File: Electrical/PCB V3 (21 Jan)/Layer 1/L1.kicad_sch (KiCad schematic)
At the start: 198 parts, among them J1 Conn_01x02, J3 Conn_01x02, SW1 SW_SPDT, U2 CD74HC4067SM, U3 CD74HC4067SM, U4 XT30UPB-M, U5 113991054

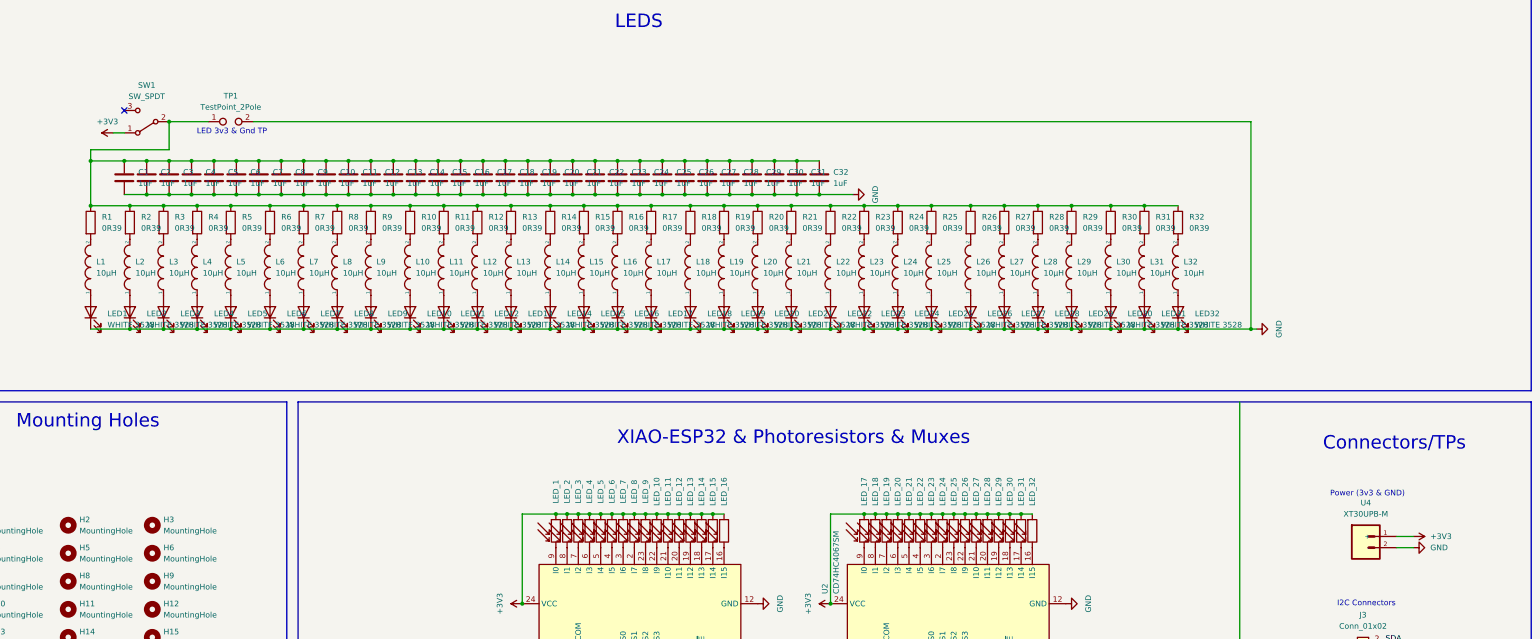
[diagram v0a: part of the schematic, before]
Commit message: added l2 dxf v4, started on l1 again
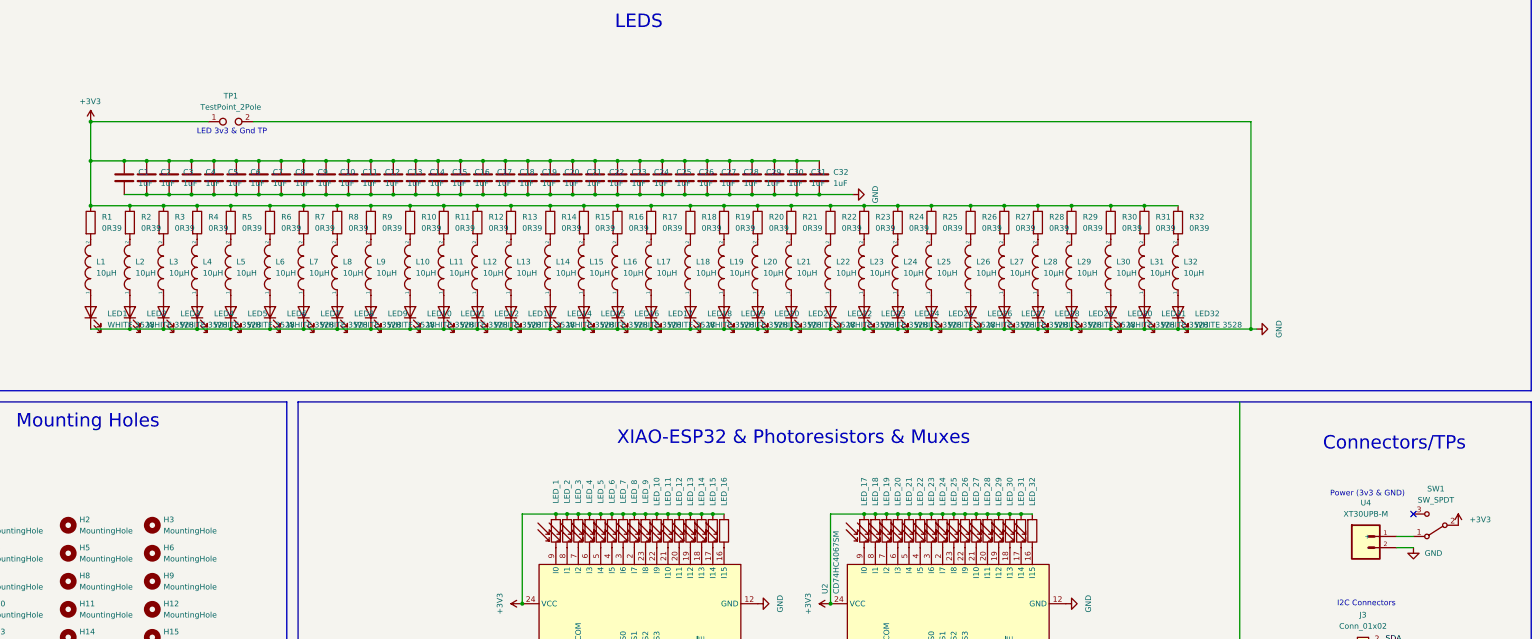
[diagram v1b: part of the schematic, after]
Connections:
- net +3V3: now also C1.1, C10.1, C11.1, C12.1, C13.1, C14.1, C15.1, C16.1, C17.1, C18.1, C19.1, C2.1, C20.1, C21.1, C22.1, C23.1, C24.1, C25.1, C26.1, C27.1, C28.1, C29.1, C3.1, C30.1, C31.1, C32.1, C4.1, C5.1, C6.1, C7.1, C8.1, C9.1, R1.1, R10.1, R11.1, R12.1, R13.1, R14.1, R15.1, R16.1, R17.1, R18.1, R19.1, R2.1, R20.1, R21.1, R22.1, R23.1, R24.1, R25.1, R26.1, R27.1, R28.1, R29.1, R3.1, R30.1, R31.1, R32.1, R4.1, R5.1, R6.1, R7.1, R8.1, R9.1, SW1.2 (B), TP1.1; no longer SW1.1 (A), U4.1 (+)
- new net: SW1.1 (A), U4.1 (+)
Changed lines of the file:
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@@
 	)
 	(junction
-		(at 90.17 53.34)
-		(diameter 0)
-		(color 0 0 0 0)
-	)
-	(junction
 		(at 191.77 62.23)
 		(diameter 0)
@@
 	)
 	(junction
+		(at 72.39 53.34)
+		(diameter 0)
+		(color 0 0 0 0)
+	)
+	(junction
 		(at 283.21 142.24)
 		(diameter 0)
@@
 	)
 	(no_connect
-		(at 80.01 50.8)
-	)
-	(no_connect
 		(at 210.82 175.26)
 	)
@@
 		(at 245.11 218.44)
 	)
+	(no_connect
+		(at 372.11 142.24)
+	)
 	(wire
 		(pts
@@
 	(wire
 		(pts
-			(xy 72.39 59.69) (xy 90.17 59.69)
-		)
-		(stroke
-			(width 0)
-			(type default)
-		)
-	)
-	(wire
-		(pts
-			(xy 99.06 53.34) (xy 90.17 53.34)
-		)
-		(stroke
-			(width 0)
-			(type default)
-		)
-	)
-	(wire
-		(pts
 			(xy 120.65 69.85) (xy 125.73 69.85)
 		)
@@
 	(wire
 		(pts
-			(xy 90.17 53.34) (xy 90.17 59.69)
-		)
-		(stroke
-			(width 0)
-			(type default)
-		)
-	)
-	(wire
-		(pts
 			(xy 88.9 100.33) (xy 96.52 100.33)
 		)
@@
 	(wire
 		(pts
-			(xy 72.39 59.69) (xy 72.39 62.23)
+			(xy 72.39 53.34) (xy 72.39 62.23)
 		)
 		(stroke
@@
 	(wire
 		(pts
+			(xy 72.39 53.34) (xy 99.06 53.34)
+		)
+		(stroke
+			(width 0)
+			(type default)
+		)
+	)
+	(wire
+		(pts
 			(xy 335.28 100.33) (xy 336.55 100.33)
 		)
@@
 	(wire
 		(pts
-			(xy 77.47 55.88) (xy 80.01 55.88)
-		)
-		(stroke
-			(width 0)
-			(type default)
-		)
-	)
-	(wire
-		(pts
 			(xy 191.77 72.39) (xy 199.39 72.39)
 		)
@@
 	)
 	(symbol
+		(lib_id "Switch:SW_SPDT")
+		(at 377.19 144.78 180)
+		(unit 1)
+		(exclude_from_sim no)
+		(in_bom yes)
+		(on_board yes)
+		(dnp no)
+		(fields_autoplaced yes)
+		(property "Reference" "SW1"
+			(at 377.19 136.525 0)
+			(effects
+				(font
+					(size 1.27 1.27)
+				)
+			)
+		)
+		(property "Value" "SW_SPDT"
+			(at 377.19 139.065 0)
+			(effects
+				(font
+					(size 1.27 1.27)
+				)
+			)
+		)
+		(property "Footprint" "Button_Switch_SMD:Nidec_Copal_CAS-120A"
+			(at 377.19 144.78 0)
+			(effects
+				(font
+					(size 1.27 1.27)
+				)
+				(hide yes)
+			)
+		)
+		(property "Datasheet" "~"
+			(at 377.19 144.78 0)
+			(effects
+				(font
+					(size 1.27 1.27)
+				)
+				(hide yes)
+			)
+		)
+		(property "Description" ""
+			(at 377.19 144.78 0)
+			(effects
+				(font
+					(size 1.27 1.27)
+				)
+				(hide yes)
+			)
+		)
+		(pin "2"
+		)
+		(pin "1"
+		)
+		(pin "3"
+		)
+		(instances
+			(project "L1"
+				(path "/9e8a7821-ee65-4356-a785-1f444d794ef4"
+					(reference "SW1")
+					(unit 1)
+				)
+			)
+		)
+	)
+	(symbol
 		(lib_id "Device:R_Photo")
 		(at 180.34 146.05 0)
@@
 	(symbol
 		(lib_id "power:+3V3")
-		(at 372.11 147.32 270)
+		(at 382.27 144.78 0)
 		(unit 1)
 		(exclude_from_sim no)
@@
 		(fields_autoplaced yes)
 		(property "Reference" "#PWR03"
-			(at 368.3 147.32 0)
+			(at 382.27 148.59 0)
 			(effects
 				(font
@@
 		)
 		(property "Value" "+3V3"
-			(at 375.92 147.3199 90)
+			(at 384.81 143.5099 0)
 			(effects
 				(font
@@
 		)
 		(property "Footprint" ""
-			(at 372.11 147.32 0)
+			(at 382.27 144.78 0)
 			(effects
 				(font
@@
 		)
 		(property "Datasheet" ""
-			(at 372.11 147.32 0)
+			(at 382.27 144.78 0)
 			(effects
 				(font
@@
 		)
 		(property "Description" "Power symbol creates a global label with name \"+3V3\""
-			(at 372.11 147.32 0)
+			(at 382.27 144.78 0)
 			(effects
 				(font
@@
 	(symbol
 		(lib_id "Library:GND")
-		(at 372.11 149.86 90)
+		(at 372.11 149.86 0)
 		(unit 1)
 		(exclude_from_sim no)
@@
 		(fields_autoplaced yes)
 		(property "Reference" "#PWR04"
-			(at 378.46 149.86 0)
+			(at 372.11 156.21 0)
 			(effects
 				(font
@@
 		)
 		(property "Value" "GND"
-			(at 375.92 149.8599 90)
+			(at 374.65 151.1299 0)
 			(effects
 				(font
 					(size 1.27 1.27)
 				)
-				(justify right)
+				(justify left)
 			)
 		)
@@
 	)
 	(symbol
-		(lib_id "Switch:SW_SPDT")
-		(at 85.09 53.34 180)
-		(unit 1)
-		(exclude_from_sim no)
-		(in_bom yes)
-		(on_board yes)
-		(dnp no)
-		(fields_autoplaced yes)
-		(property "Reference" "SW1"
-			(at 85.09 45.085 0)
-			(effects
-				(font
-					(size 1.27 1.27)
-				)
-			)
-		)
-		(property "Value" "SW_SPDT"
-			(at 85.09 47.625 0)
-			(effects
-				(font
-					(size 1.27 1.27)
-				)
-			)
-		)
-		(property "Footprint" "Button_Switch_SMD:Nidec_Copal_CAS-120A"
-			(at 85.09 53.34 0)
-			(effects
-				(font
-					(size 1.27 1.27)
-				)
-				(hide yes)
-			)
-		)
-		(property "Datasheet" "~"
-			(at 85.09 53.34 0)
-			(effects
-				(font
-					(size 1.27 1.27)
-				)
-				(hide yes)
-			)
-		)
-		(property "Description" ""
-			(at 85.09 53.34 0)
-			(effects
-				(font
-					(size 1.27 1.27)
-				)
-				(hide yes)
-			)
-		)
-		(pin "2"
-		)
-		(pin "1"
-		)
-		(pin "3"
-		)
-		(instances
-			(project "l1 v1"
-				(path "/9e8a7821-ee65-4356-a785-1f444d794ef4"
-					(reference "SW1")
-					(unit 1)
-				)
-			)
-		)
-	)
-	(symbol
 		(lib_id "Device:C")
 		(at 135.89 66.04 0)
@@
 	(symbol
 		(lib_id "power:+3V3")
-		(at 77.47 55.88 90)
+		(at 72.39 53.34 0)
 		(unit 1)
 		(exclude_from_sim no)
@@
 		(on_board yes)
 		(dnp no)
-		(fields_autoplaced yes)
 		(property "Reference" "#PWR09"
-			(at 81.28 55.88 0)
+			(at 72.39 57.15 0)
 			(effects
 				(font
@@
 		)
 		(property "Value" "+3V3"
-			(at 76.2 53.34 90)
+			(at 69.85 48.768 0)
 			(effects
 				(font
 					(size 1.27 1.27)
 				)
+				(justify left)
 			)
 		)
 		(property "Footprint" ""
-			(at 77.47 55.88 0)
+			(at 72.39 53.34 0)
 			(effects
 				(font
@@
 		)
 		(property "Datasheet" ""
-			(at 77.47 55.88 0)
+			(at 72.39 53.34 0)
 			(effects
 				(font
@@
 		)
 		(property "Description" "Power symbol creates a global label with name \"+3V3\""
-			(at 77.47 55.88 0)
+			(at 72.39 53.34 0)
 			(effects
 				(font

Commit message: finished l1?
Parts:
- J1, J3, TP1: footprint Connector_PinHeader_1.00mm:PinHeader_1x02_P1.00mm_Vertical -> Connector_PinHeader_2.54mm:PinHeader_1x02_P2.54mm_Vertical
- R33, R34: footprint Resistor_SMD:R_0201_0603Metric -> Resistor_SMD:R_0603_1608Metric
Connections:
- net Mux Com (1-16): now also R34.2, U3.1 (COM), U5.2 (D1); no longer R33.2, U2.1 (COM), U5.1 (D0)
- net Mux Com (17-32): now also R33.2, U2.1 (COM), U5.1 (D0); no longer R34.2, U3.1 (COM), U5.2 (D1)
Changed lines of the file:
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@@
 	)
 	(label "Mux Com (17-32)"
-		(at 175.26 175.26 270)
+		(at 245.11 176.53 270)
 		(effects
 			(font
@@
 	)
 	(label "Mux Com (17-32)"
-		(at 209.55 215.9 180)
+		(at 209.55 213.36 180)
 		(effects
 			(font
@@
 	)
 	(label "Mux Com (1-16)"
-		(at 209.55 213.36 180)
+		(at 209.55 215.9 180)
 		(effects
 			(font
@@
 	)
 	(label "Mux Com (1-16)"
-		(at 245.11 176.53 270)
+		(at 175.26 175.26 270)
 		(effects
 			(font
@@
 			)
 		)
-		(property "Footprint" "Resistor_SMD:R_0201_0603Metric"
+		(property "Footprint" "Resistor_SMD:R_0603_1608Metric"
 			(at 184.658 179.07 90)
 			(effects
@@
 			)
 		)
-		(property "Footprint" "Connector_PinHeader_1.00mm:PinHeader_1x02_P1.00mm_Vertical"
+		(property "Footprint" "Connector_PinHeader_2.54mm:PinHeader_1x02_P2.54mm_Vertical"
 			(at 104.14 53.34 0)
 			(effects
@@
 			)
 		)
-		(property "Footprint" "Resistor_SMD:R_0201_0603Metric"
+		(property "Footprint" "Resistor_SMD:R_0603_1608Metric"
 			(at 254.508 180.34 90)
 			(effects
@@
 			)
 		)
-		(property "Footprint" "Connector_PinHeader_1.00mm:PinHeader_1x02_P1.00mm_Vertical"
+		(property "Footprint" "Connector_PinHeader_2.54mm:PinHeader_1x02_P2.54mm_Vertical"
 			(at 360.68 196.85 0)
 			(effects
@@
 			)
 		)
-		(property "Footprint" "Connector_PinHeader_1.00mm:PinHeader_1x02_P1.00mm_Vertical"
+		(property "Footprint" "Connector_PinHeader_2.54mm:PinHeader_1x02_P2.54mm_Vertical"
 			(at 360.68 173.99 0)
 			(effects

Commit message: finished layer1?
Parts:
- added C33, C34: C, Capacitor_SMD:C_0603_1608Metric, symbol Device:C
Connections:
- net +3V3: now also C33.1, C34.1; no longer U2.24 (VCC), U3.24 (VCC)
- new net: C33.2, U3.24 (VCC)
- new net: C34.2, U2.24 (VCC)
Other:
- moved on the sheet: LED_1, LED_10, LED_11, LED_12, LED_13, LED_14, LED_15, LED_16, LED_17, LED_18, LED_19, LED_2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

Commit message: added l3 v3 dxf, did somemore l1
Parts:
- removed J1, J3: Conn_01x02, Connector_PinHeader_2.54mm:PinHeader_1x02_P2.54mm_Vertical, symbol Connector_Generic:Conn_01x02
- removed SW1: SW_SPDT, Button_Switch_SMD:Nidec_Copal_CAS-120A, symbol Switch:SW_SPDT
- removed U4: XT30UPB-M, Connector_AMASS:AMASS_XT30U-M_1x02_P5.0mm_Vertical, symbol XT30UPB-M:XT30UPB-M
- added J1: Conn_01x04, Connector_JST:JST_EH_B4B-EH-A_1x04_P2.50mm_Vertical, symbol Connector_Generic:Conn_01x04
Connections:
- net +3V3: now also J1.4 (Pin_4)
- net GND: now also J1.1 (Pin_1)
- net SCL: no longer names the net of U5.6 (D5)
- net SDA: no longer names the net of U5.5 (D4)
- net UART (RX) renamed L1 RX
- net L1 RX: now also J1.3 (Pin_3)
- net UART (TX) renamed L1 TX
- net L1 TX: now also J1.2 (Pin_2)
- no-connect marks 5 -> 6
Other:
- note removed: "I2C Connectors"

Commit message: did somemore l1
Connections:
- net +3V3: now also C33.2, C34.2, U2.24 (VCC), U3.24 (VCC); no longer C33.1, C34.1
- net GND: now also C33.1, C34.1

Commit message: pls no conflict
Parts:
- removed J1: Conn_01x04, Connector_JST:JST_EH_B4B-EH-A_1x04_P2.50mm_Vertical, symbol Connector_Generic:Conn_01x04
- added C35, C38: 0u1, Capacitor_THT:CP_Axial_L10.0mm_D6.0mm_P15.00mm_Horizontal, symbol Device:C
- added C36: 100u, Capacitor_THT:CP_Axial_L10.0mm_D6.0mm_P15.00mm_Horizontal, symbol Device:C_Polarized
- added C37: 1u, Capacitor_THT:CP_Axial_L10.0mm_D6.0mm_P15.00mm_Horizontal, symbol Device:C
- added C39: 220uF, Capacitor_THT:CP_Axial_L10.0mm_D6.0mm_P15.00mm_Horizontal, symbol Device:C_Polarized
- added D1: SS510, Capacitor_SMD:C_0603_1608Metric, symbol Device:D_Schottky
- added J1: Conn_01x05, Connector_PinHeader_2.54mm:PinHeader_1x05_P2.54mm_Vertical, symbol Connector_Generic:Conn_01x05
- added L33: 68uH, Inductor_SMD:L_APV_APH1040, symbol Device:L
- added R35: 2k94, Sen Robo:res0603, symbol Device:R
- added R36: 57K, Sen Robo:res0603, symbol Device:R
- added R37: 1K5, Sen Robo:res0603, symbol Device:R
- added U1: LM2587S-ADJ, layer2v3:VREG_LM5017MR_NOPB, symbol lm2587(boost):LM2587S-ADJ
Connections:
- net +3V3: now also J1.5 (Pin_5)
- net GND: now also C35.2, C36.2, C37.2, C38.2, C39.2, J1.1 (Pin_1), R37.2, U1.3 (GND), U1.6 (GND)
- net L1 RX: now also J1.4 (Pin_4)
- net L1 TX: now also J1.3 (Pin_3)
- new net: R36.2, R37.1, U1.2 (FB)
- new net: R35.1, U1.1 (COMP)
- new net: D1.2 (A), L33.2, U1.4 (SW)
- new net: C37.1, R35.2
- new net +12V: C35.1, C36.1, J1.2 (Pin_2), L33.1, U1.5 (VIN)
- new net +24V: C38.1, C39.1, D1.1 (K), R36.1
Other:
- note added: "Bost:C"
- note added: "Power (12v)"

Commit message: fixed?
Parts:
- added U4: XT30UPB-M, layer2v3:XT30UPB-M, symbol amass xt 30:XT30UPB-M
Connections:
- net +12V: now also J1.3 (Pin_3); no longer J1.2 (Pin_2)
- net +24V: now also U4.P$1 (+)
- net GND: now also U4.P$2 (-)
- net L1 TX: now also J1.2 (Pin_2); no longer J1.3 (Pin_3)

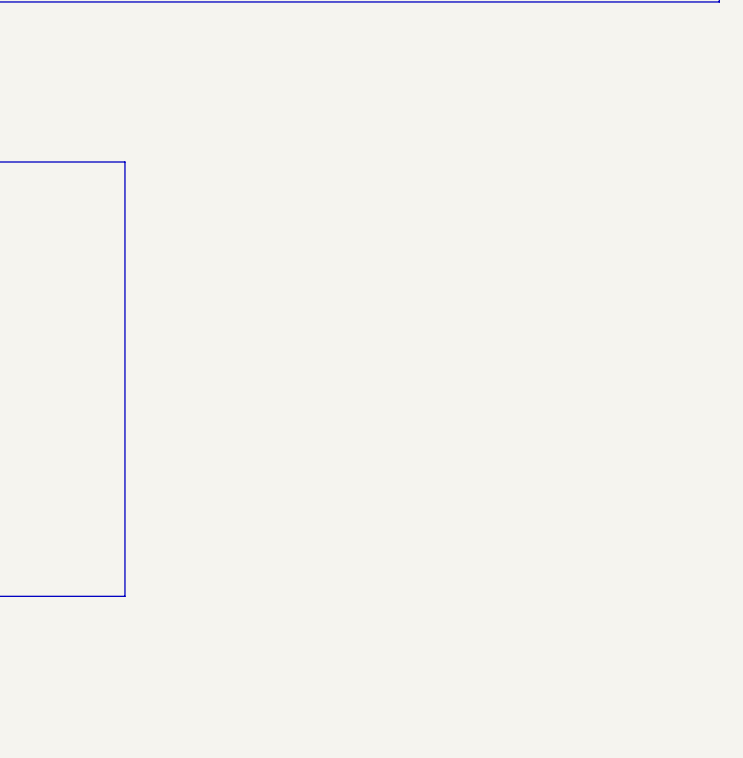
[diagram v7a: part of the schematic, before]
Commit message: touched up with test points and shared l2 with  haoyun
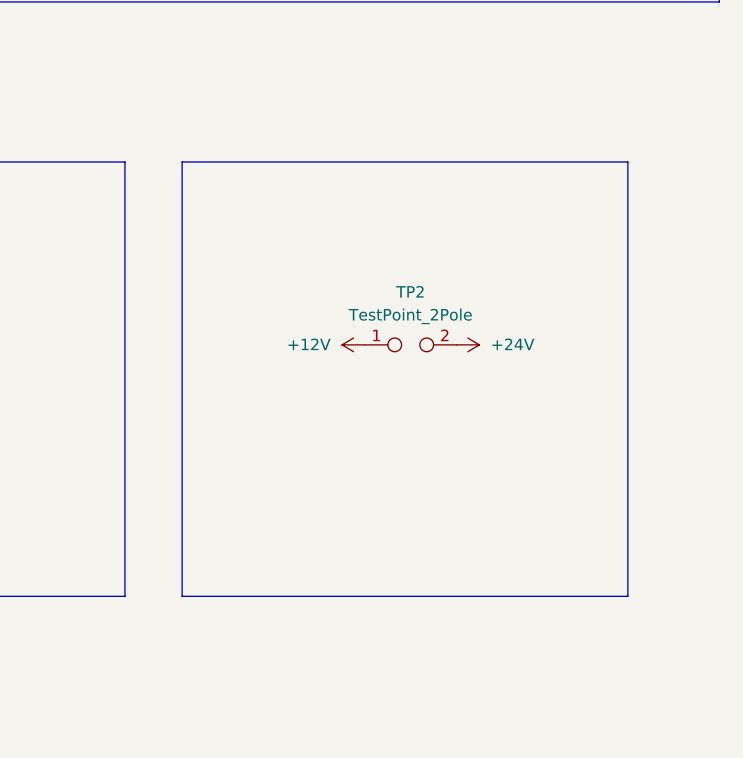
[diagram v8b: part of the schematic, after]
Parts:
- added TP2: TestPoint_2Pole, Connector_PinHeader_2.54mm:PinHeader_1x02_P2.54mm_Vertical, symbol Connector:TestPoint_2Pole
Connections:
- net +12V: now also TP2.1
- net +24V: now also TP2.2
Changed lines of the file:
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@@
 		)
 	)
+	(rectangle
+		(start 461.01 115.57)
+		(end 510.54 163.83)
+		(stroke
+			(width 0)
+			(type default)
+		)
+		(fill
+			(type none)
+		)
+	)
 	(text_box "Mounting Holes"
 		(exclude_from_sim no)
@@
 	)
 	(symbol
+		(lib_id "power:+12V")
+		(at 481.33 135.89 90)
+		(unit 1)
+		(exclude_from_sim no)
+		(in_bom yes)
+		(on_board yes)
+		(dnp no)
+		(fields_autoplaced yes)
+		(property "Reference" "#PWR024"
+			(at 485.14 135.89 0)
+			(effects
+				(font
+					(size 1.27 1.27)
+				)
+				(hide yes)
+			)
+		)
+		(property "Value" "+12V"
+			(at 477.52 135.8899 90)
+			(effects
+				(font
+					(size 1.27 1.27)
+				)
+				(justify left)
+			)
+		)
+		(property "Footprint" ""
+			(at 481.33 135.89 0)
+			(effects
+				(font
+					(size 1.27 1.27)
+				)
+				(hide yes)
+			)
+		)
+		(property "Datasheet" ""
+			(at 481.33 135.89 0)
+			(effects
+				(font
+					(size 1.27 1.27)
+				)
+				(hide yes)
+			)
+		)
+		(property "Description" "Power symbol creates a global label with name \"+12V\""
+			(at 481.33 135.89 0)
+			(effects
+				(font
+					(size 1.27 1.27)
+				)
+				(hide yes)
+			)
+		)
+		(pin "1"
+		)
+		(instances
+			(project ""
+				(path "/9e8a7821-ee65-4356-a785-1f444d794ef4"
+					(reference "#PWR024")
+					(unit 1)
+				)
+			)
+		)
+	)
+	(symbol
 		(lib_id "Device:R_Photo")
 		(at 283.21 146.05 0)
@@
 	)
 	(symbol
+		(lib_id "Connector:TestPoint_2Pole")
+		(at 486.41 135.89 0)
+		(unit 1)
+		(exclude_from_sim no)
+		(in_bom yes)
+		(on_board yes)
+		(dnp no)
+		(property "Reference" "TP2"
+			(at 486.41 130.048 0)
+			(effects
+				(font
+					(size 1.27 1.27)
+				)
+			)
+		)
+		(property "Value" "TestPoint_2Pole"
+			(at 486.41 132.588 0)
+			(effects
+				(font
+					(size 1.27 1.27)
+				)
+			)
+		)
+		(property "Footprint" "Connector_PinHeader_2.54mm:PinHeader_1x02_P2.54mm_Vertical"
+			(at 486.41 135.89 0)
+			(effects
+				(font
+					(size 1.27 1.27)
+				)
+				(hide yes)
+			)
+		)
+		(property "Datasheet" "~"
+			(at 486.41 135.89 0)
+			(effects
+				(font
+					(size 1.27 1.27)
+				)
+				(hide yes)
+			)
+		)
+		(property "Description" "2-polar test point"
+			(at 486.41 135.89 0)
+			(effects
+				(font
+					(size 1.27 1.27)
+				)
+				(hide yes)
+			)
+		)
+		(pin "1"
+		)
+		(pin "2"
+		)
+		(instances
+			(project "L1"
+				(path "/9e8a7821-ee65-4356-a785-1f444d794ef4"
+					(reference "TP2")
+					(unit 1)
+				)
+			)
+		)
+	)
+	(symbol
 		(lib_id "pspice:INDUCTOR")
 		(at 176.53 86.36 90)
@@
 					(unit 1)
 				)
+			)
+		)
+	)
+	(symbol
+		(lib_id "power:+24V")
+		(at 491.49 135.89 270)
+		(unit 1)
+		(exclude_from_sim no)
+		(in_bom yes)
+		(on_board yes)
+		(dnp no)
+		(fields_autoplaced yes)
+		(property "Reference" "#PWR025"
+			(at 487.68 135.89 0)
+			(effects
+				(font
+					(size 1.27 1.27)
+				)
+				(hide yes)
+			)
+		)
+		(property "Value" "+24V"
+			(at 495.3 135.8899 90)
+			(effects
+				(font
+					(size 1.27 1.27)
+				)
+				(justify left)
+			)
+		)
+		(property "Footprint" ""
+			(at 491.49 135.89 0)
+			(effects
+				(font
+					(size 1.27 1.27)
+				)
+				(hide yes)
+			)
+		)
+		(property "Datasheet" ""
+			(at 491.49 135.89 0)
+			(effects
+				(font
+					(size 1.27 1.27)
+				)
+				(hide yes)
+			)
+		)
+		(property "Description" "Power symbol creates a global label with name \"+24V\""
+			(at 491.49 135.89 0)
+			(effects
+				(font
+					(size 1.27 1.27)
+				)
+				(hide yes)
+			)
+		)
+		(pin "1"
+		)
+		(instances
+			(project ""
+				(path "/9e8a7821-ee65-4356-a785-1f444d794ef4"
+					(reference "#PWR025")
+					(unit 1)
+				)
